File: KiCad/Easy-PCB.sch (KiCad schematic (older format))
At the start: 20 parts, among them J1 703W-00/53, J3 HLW20R-2C7LF, P1 Molex 0022032021, P2 Molex 0901200126, P3 Molex 0022032041, P4 Molex 387203208, P5 Molex 0022032021, Q1 2N3904, SW1 DF62J12S2AHQA, U1 PIC16F883

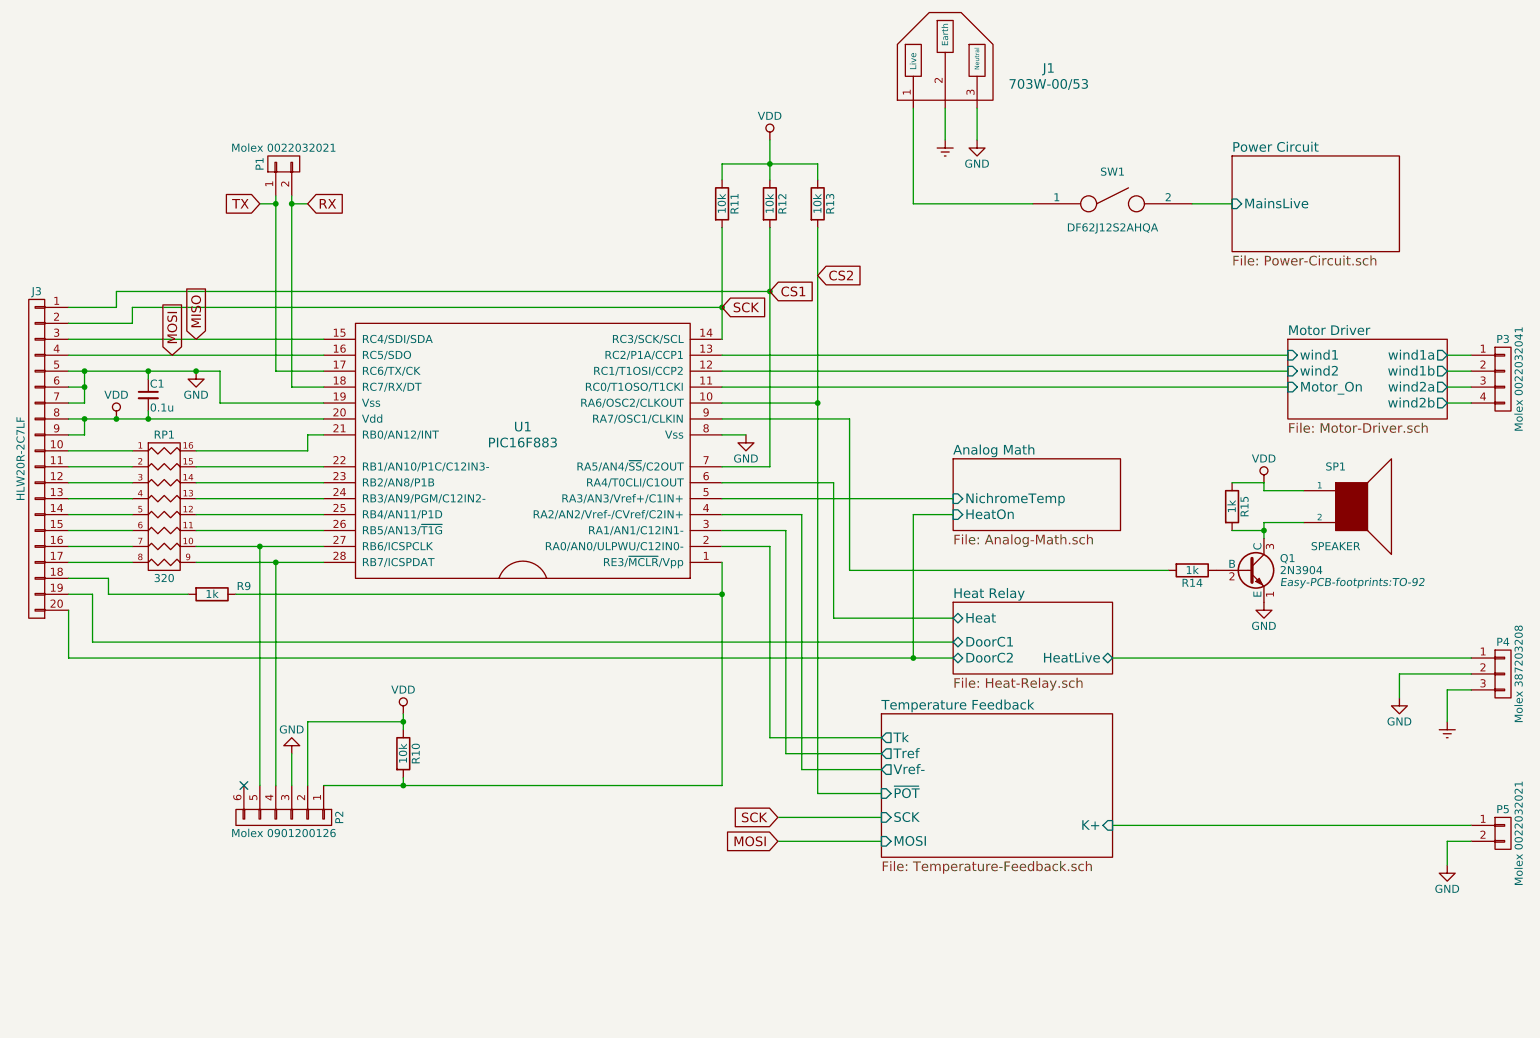
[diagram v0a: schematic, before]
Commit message: footprint associations complete
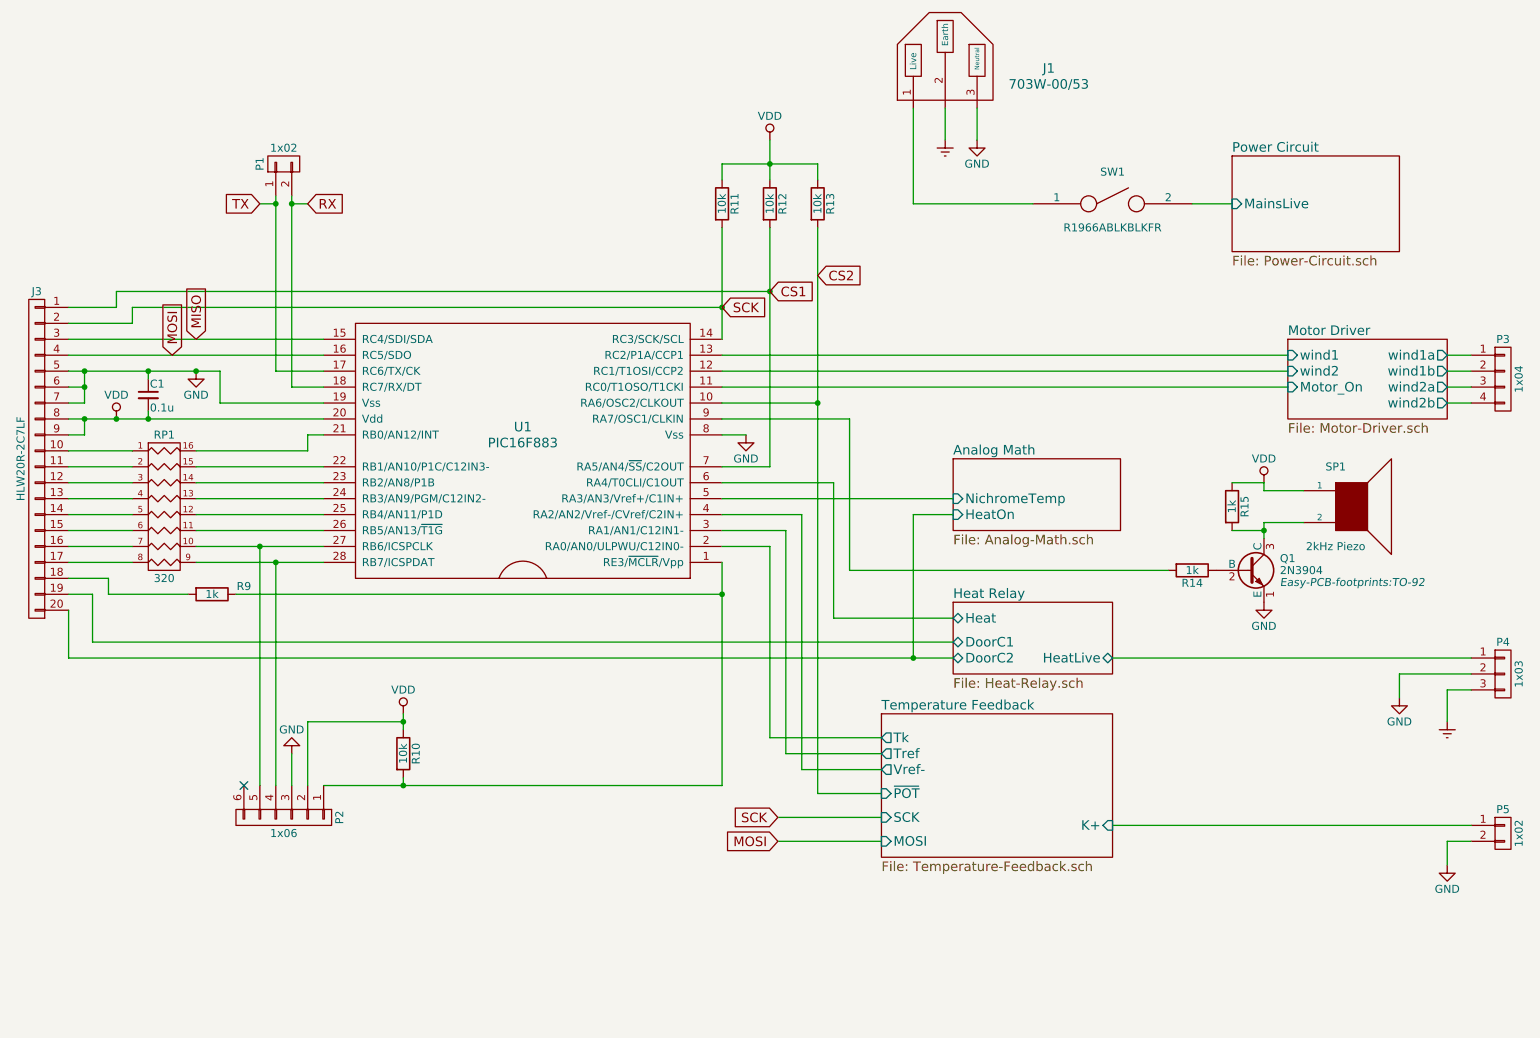
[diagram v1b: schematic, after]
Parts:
- J1: footprint (none) -> Easy-PCB-footprints:703W-0053
- P1, P5: value Molex 0022032021 -> 1x02; footprint (none) -> Socket_Strips:Socket_Strip_Straight_1x02
- P2: value Molex 0901200126 -> 1x06; footprint (none) -> Socket_Strips:Socket_Strip_Straight_1x06
- P3: value Molex 0022032041 -> 1x04; footprint (none) -> Socket_Strips:Socket_Strip_Straight_1x04
- P4: value Molex 387203208 -> 1x03; footprint (none) -> Socket_Strips:Socket_Strip_Straight_1x03
- SP1: value SPEAKER -> 2kHz Piezo; footprint (none) -> Easy-PCB-footprints:PS1420
- SW1: value DF62J12S2AHQA -> R1966ABLKBLKFR; footprint (none) -> Easy-PCB-footprints:R1966ABLKBLKFR
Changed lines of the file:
@@
 P 2550 1800
 F 0 "P1" H 2550 1950 50  0000 C CNN
-F 1 "Molex 0022032021" V 2650 1800 50  0000 C CNN
-F 2 "" H 2550 1800 50  0001 C CNN
+F 1 "1x02" V 2650 1800 50  0000 C CNN
+F 2 "Socket_Strips:Socket_Strip_Straight_1x02" H 2550 1800 50  0001 C CNN
 F 3 "" H 2550 1800 50  0000 C CNN
 	1    2550 1800
@@
 P 2550 5900
 F 0 "P2" H 2550 6250 50  0000 C CNN
-F 1 "Molex 0901200126" V 2650 5900 50  0000 C CNN
-F 2 "" H 2550 5900 50  0001 C CNN
+F 1 "1x06" V 2650 5900 50  0000 C CNN
+F 2 "Socket_Strips:Socket_Strip_Straight_1x06" H 2550 5900 50  0001 C CNN
 F 3 "" H 2550 5900 50  0000 C CNN
 	1    2550 5900
@@
 P 9250 3950
 F 0 "SP1" H 9150 4200 50  0000 C CNN
-F 1 "SPEAKER" H 9150 3700 50  0000 C CNN
-F 2 "" H 9250 3950 50  0001 C CNN
+F 1 "2kHz Piezo" H 9150 3700 50  0000 C CNN
+F 2 "Easy-PCB-footprints:PS1420" H 9250 3950 50  0001 C CNN
 F 3 "" H 9250 3950 50  0000 C CNN
 	1    9250 3950
@@
 P 10200 3150
 F 0 "P3" H 10200 3400 50  0000 C CNN
-F 1 "Molex 0022032041" V 10300 3150 50  0000 C CNN
-F 2 "" H 10200 3150 50  0001 C CNN
+F 1 "1x04" V 10300 3150 50  0000 C CNN
+F 2 "Socket_Strips:Socket_Strip_Straight_1x04" H 10200 3150 50  0001 C CNN
 F 3 "" H 10200 3150 50  0000 C CNN
 	1    10200 3150
@@
 F 0 "J1" H 7350 1400 60  0000 C CNN
 F 1 "703W-00/53" H 7350 1300 60  0000 C CNN
-F 2 "" H 6700 1300 60  0001 C CNN
+F 2 "Easy-PCB-footprints:703W-0053" H 6700 1300 60  0001 C CNN
 F 3 "" H 6700 1300 60  0000 C CNN
 	1    6700 1300
@@
 P 7750 2050
 F 0 "SW1" H 7750 2250 50  0000 C CNN
-F 1 "DF62J12S2AHQA" H 7750 1900 50  0000 C CNN
-F 2 "" H 7750 2050 50  0001 C CNN
+F 1 "R1966ABLKBLKFR" H 7750 1900 50  0000 C CNN
+F 2 "Easy-PCB-footprints:R1966ABLKBLKFR" H 7750 2050 50  0001 C CNN
 F 3 "" H 7750 2050 50  0000 C CNN
 	1    7750 2050
@@
 P 10200 6000
 F 0 "P5" H 10200 6150 50  0000 C CNN
-F 1 "Molex 0022032021" V 10300 6000 50  0000 C CNN
-F 2 "" H 10200 6000 50  0001 C CNN
+F 1 "1x02" V 10300 6000 50  0000 C CNN
+F 2 "Socket_Strips:Socket_Strip_Straight_1x02" H 10200 6000 50  0001 C CNN
 F 3 "" H 10200 6000 50  0000 C CNN
 	1    10200 6000
@@
 P 10200 5000
 F 0 "P4" H 10200 5200 50  0000 C CNN
-F 1 "Molex 387203208" V 10300 5000 50  0000 C CNN
-F 2 "" H 10200 5000 50  0001 C CNN
+F 1 "1x03" V 10300 5000 50  0000 C CNN
+F 2 "Socket_Strips:Socket_Strip_Straight_1x03" H 10200 5000 50  0001 C CNN
 F 3 "" H 10200 5000 50  0000 C CNN
 	1    10200 5000

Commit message: errors cleared and components on board
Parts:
- C1: footprint Capacitors_ThroughHole:C_Disc_D3_P2.5 -> Easy-PCB-footprints:C_Disc_D3_P2.5
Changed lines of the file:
@@
 F 0 "C1" H 1710 3320 50  0000 L CNN
 F 1 "0.1u" H 1710 3170 50  0000 L CNN
-F 2 "Capacitors_ThroughHole:C_Disc_D3_P2.5" H 1700 3250 50  0001 C CNN
+F 2 "Easy-PCB-footprints:C_Disc_D3_P2.5" H 1700 3250 50  0001 C CNN
 F 3 "" H 1700 3250 50  0000 C CNN
 	1    1700 3250

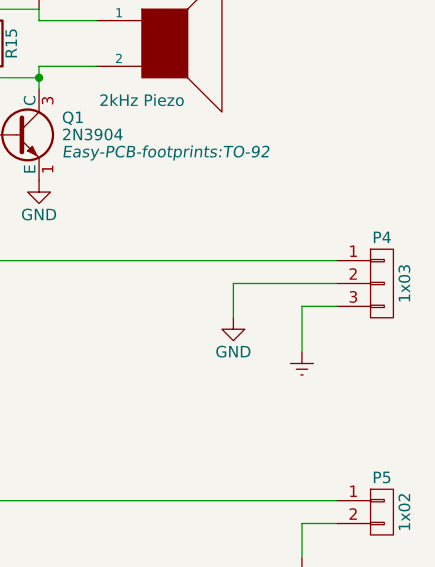
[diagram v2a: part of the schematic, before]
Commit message: power supply placed and routed
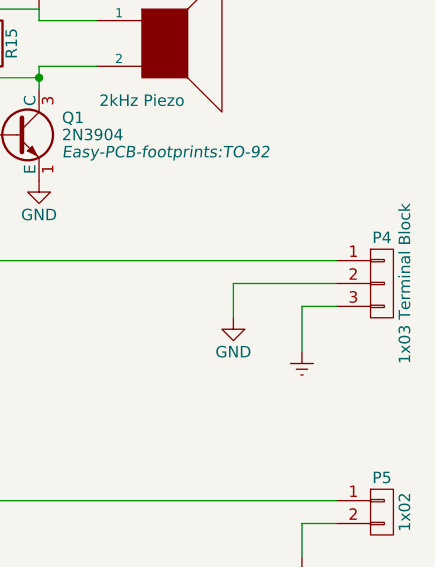
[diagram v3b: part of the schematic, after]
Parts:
- P4: value 1x03 -> 1x03 Terminal Block; footprint Socket_Strips:Socket_Strip_Straight_1x03 -> Easy-PCB-footprints:5-1437652-4
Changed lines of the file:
@@
 P 10200 5000
 F 0 "P4" H 10200 5200 50  0000 C CNN
-F 1 "1x03" V 10300 5000 50  0000 C CNN
-F 2 "Socket_Strips:Socket_Strip_Straight_1x03" H 10200 5000 50  0001 C CNN
+F 1 "1x03 Terminal Block" V 10300 5000 50  0000 C CNN
+F 2 "Easy-PCB-footprints:5-1437652-4" H 10200 5000 50  0001 C CNN
 F 3 "" H 10200 5000 50  0000 C CNN
 	1    10200 5000

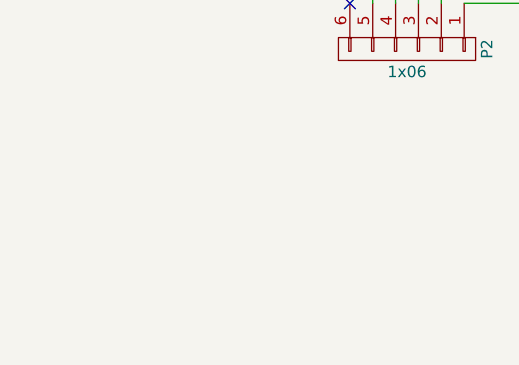
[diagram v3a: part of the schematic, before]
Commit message: motor circuit routed
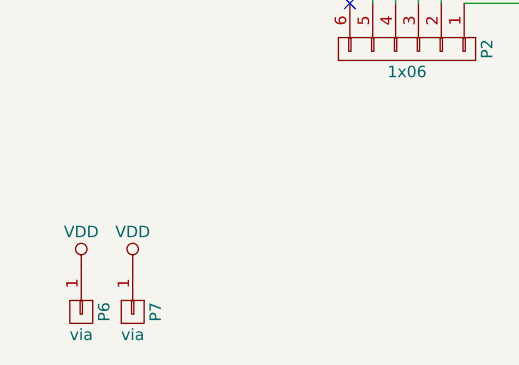
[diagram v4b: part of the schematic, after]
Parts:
- added P6, P7: via, Connect:PINTST, symbol CONN_01X01
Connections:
- net VDD: now also P6.1 (P1), P7.1 (P1)
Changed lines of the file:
@@
+	1    0    0    -1
+$EndComp
+$Comp
+L CONN_01X01 P6
+U 1 1 568D89CB
+P 1125 7050
+F 0 "P6" H 1125 7150 50  0000 C CNN
+F 1 "via" V 1225 7050 50  0000 C CNN
+F 2 "Connect:PINTST" H 1125 7050 50  0001 C CNN
+F 3 "" H 1125 7050 50  0000 C CNN
+	1    1125 7050
+	0    1    1    0
+$EndComp
+$Comp
+L CONN_01X01 P7
+U 1 1 568D8D16
+P 1350 7050
+F 0 "P7" H 1350 7150 50  0000 C CNN
+F 1 "via" V 1450 7050 50  0000 C CNN
+F 2 "Connect:PINTST" H 1350 7050 50  0001 C CNN
+F 3 "" H 1350 7050 50  0000 C CNN
+	1    1350 7050
+	0    1    1    0
+$EndComp
+$Comp
+L VDD #PWR014
+U 1 1 568D9243
+P 1125 6850
+F 0 "#PWR014" H 1125 6700 50  0001 C CNN
+F 1 "VDD" H 1125 7000 50  0000 C CNN
+F 2 "" H 1125 6850 50  0000 C CNN
+F 3 "" H 1125 6850 50  0000 C CNN
+	1    1125 6850
+	1    0    0    -1
+$EndComp
+$Comp
+L VDD #PWR015
+U 1 1 568D9301
+P 1350 6850
+F 0 "#PWR015" H 1350 6700 50  0001 C CNN
+F 1 "VDD" H 1350 7000 50  0000 C CNN
+F 2 "" H 1350 6850 50  0000 C CNN
+F 3 "" H 1350 6850 50  0000 C CNN
+	1    1350 6850
 	1    0    0    -1
 $EndComp

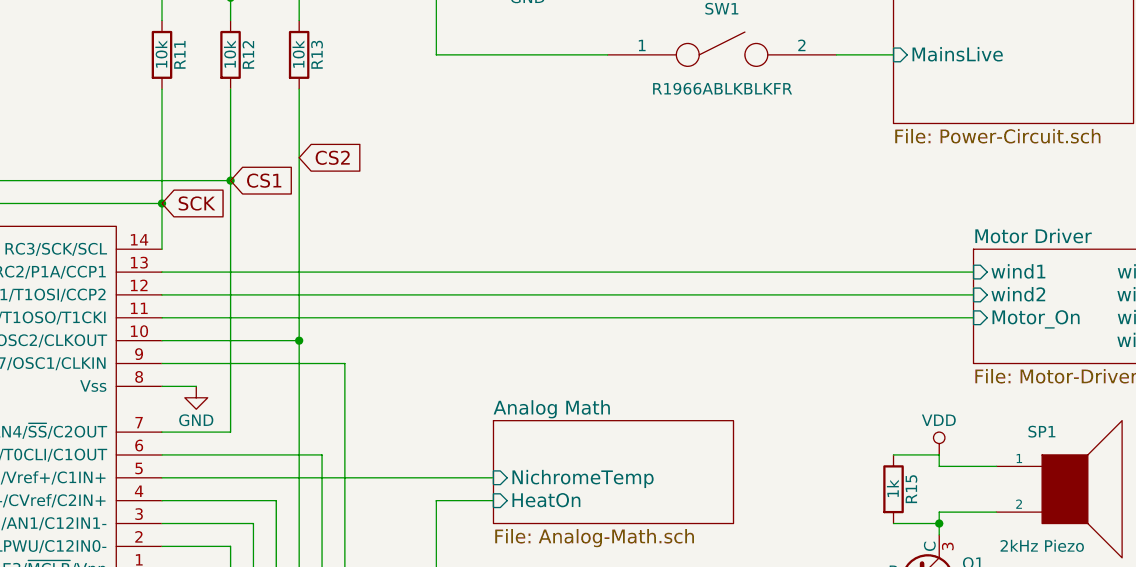
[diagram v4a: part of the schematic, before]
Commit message: reconfigured motor driver routing
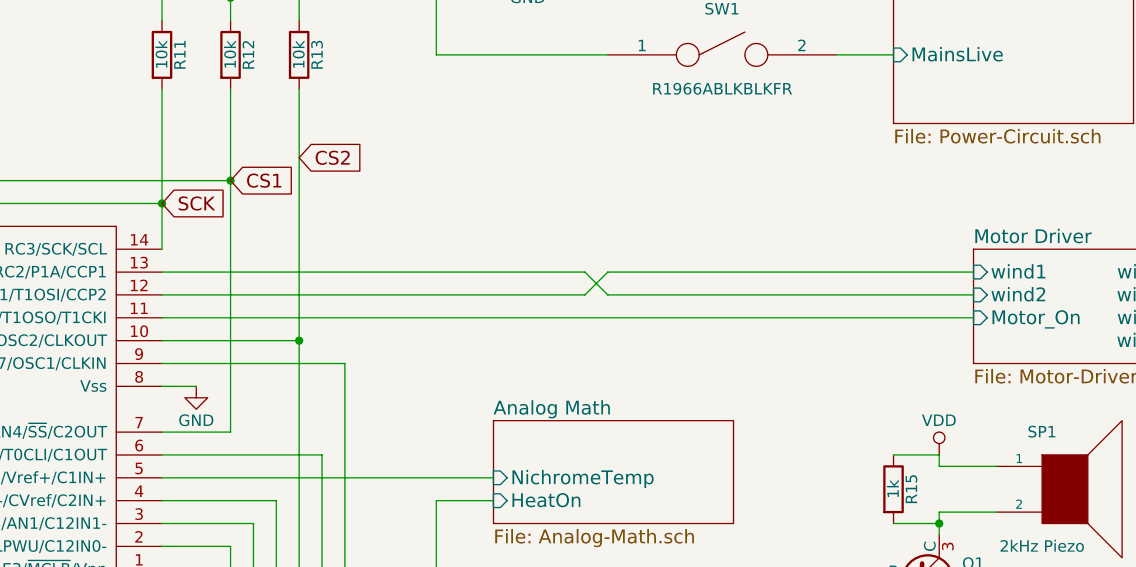
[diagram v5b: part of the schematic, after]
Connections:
- net Motor Driver/wind1: now also U1.12 (RC1/T1OSI/CCP2); no longer U1.13 (RC2/P1A/CCP1)
- net Motor Driver/wind2: now also U1.13 (RC2/P1A/CCP1); no longer U1.12 (RC1/T1OSI/CCP2)
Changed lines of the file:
@@
 	5300 3200 8850 3200
-Wire Wire Line
-	5300 3100 8850 3100
-Wire Wire Line
-	5300 3000 8850 3000
 Wire Wire Line
 	6700 1450 6700 1650
@@
 	1    0    0    -1
 $EndComp
+Wire Wire Line
+	5300 3000 7150 3000
+Wire Wire Line
+	7150 3000 7250 3100
+Wire Wire Line
+	7250 3100 8850 3100
+Wire Wire Line
+	8850 3000 7250 3000
+Wire Wire Line
+	7250 3000 7150 3100
+Wire Wire Line
+	7150 3100 5300 3100
 $EndSCHEMATC

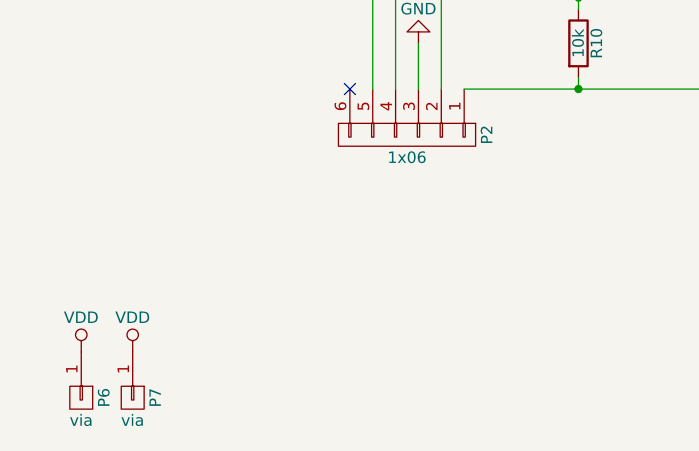
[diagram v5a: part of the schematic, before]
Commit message: connector to front PCB routed
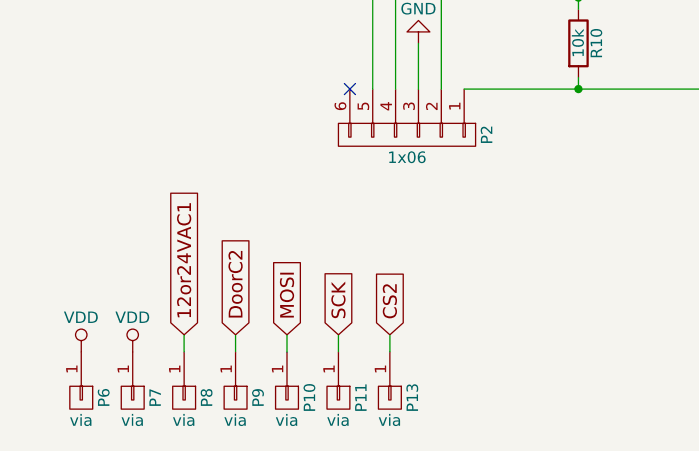
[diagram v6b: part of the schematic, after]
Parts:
- added P10, P11, P13, P8, P9: via, Connect:PINTST, symbol CONN_01X01
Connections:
- net CS2: now also P13.1 (P1)
- net MOSI: now also P10.1 (P1)
- net SCK: now also P11.1 (P1)
- new net 12or24VAC1: P8.1 (P1)
- new net DoorC2: P9.1 (P1)
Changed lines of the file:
@@
 Wire Wire Line
 	7150 3100 5300 3100
+$Comp
+L CONN_01X01 P8
+U 1 1 56A0E415
+P 1575 7050
+F 0 "P8" H 1575 7150 50  0000 C CNN
+F 1 "via" V 1675 7050 50  0000 C CNN
+F 2 "Connect:PINTST" H 1575 7050 50  0001 C CNN
+F 3 "" H 1575 7050 50  0000 C CNN
+	1    1575 7050
+	0    1    1    0
+$EndComp
+Wire Wire Line
+	1575 6850 1575 6775
+Text GLabel 1575 6775 1    60   Input ~ 0
+12or24VAC1
+$Comp
+L CONN_01X01 P9
+U 1 1 56A0EF61
+P 1800 7050
+F 0 "P9" H 1800 7150 50  0000 C CNN
+F 1 "via" V 1900 7050 50  0000 C CNN
+F 2 "Connect:PINTST" H 1800 7050 50  0001 C CNN
+F 3 "" H 1800 7050 50  0000 C CNN
+	1    1800 7050
+	0    1    1    0
+$EndComp
+Wire Wire Line
+	1800 6850 1800 6775
+Text GLabel 1800 6775 1    60   Input ~ 0
+DoorC2
+$Comp
+L CONN_01X01 P10
+U 1 1 56A104F7
+P 2025 7050
+F 0 "P10" H 2025 7150 50  0000 C CNN
+F 1 "via" V 2125 7050 50  0000 C CNN
+F 2 "Connect:PINTST" H 2025 7050 50  0001 C CNN
+F 3 "" H 2025 7050 50  0000 C CNN
+	1    2025 7050
+	0    1    1    0
+$EndComp
+Wire Wire Line
+	2025 6850 2025 6775
+Text GLabel 2025 6775 1    60   Input ~ 0
+MOSI
+$Comp
+L CONN_01X01 P11
+U 1 1 56A1147C
+P 2250 7050
+F 0 "P11" H 2250 7150 50  0000 C CNN
+F 1 "via" V 2350 7050 50  0000 C CNN
+F 2 "Connect:PINTST" H 2250 7050 50  0001 C CNN
+F 3 "" H 2250 7050 50  0000 C CNN
+	1    2250 7050
+	0    1    1    0
+$EndComp
+Wire Wire Line
+	2250 6850 2250 6775
+Text GLabel 2250 6775 1    60   Input ~ 0
+SCK
+$Comp
+L CONN_01X01 P13
+U 1 1 56A12FD6
+P 2475 7050
+F 0 "P13" H 2475 7150 50  0000 C CNN
+F 1 "via" V 2575 7050 50  0000 C CNN
+F 2 "Connect:PINTST" H 2475 7050 50  0001 C CNN
+F 3 "" H 2475 7050 50  0000 C CNN
+	1    2475 7050
+	0    1    1    0
+$EndComp
+Wire Wire Line
+	2475 6850 2475 6775
+Text GLabel 2475 6775 1    60   Input ~ 0
+CS2
 $EndSCHEMATC
